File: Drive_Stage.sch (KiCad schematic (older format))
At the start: 34 parts, among them U1 DRV8323SRTAT, U2 24LC01

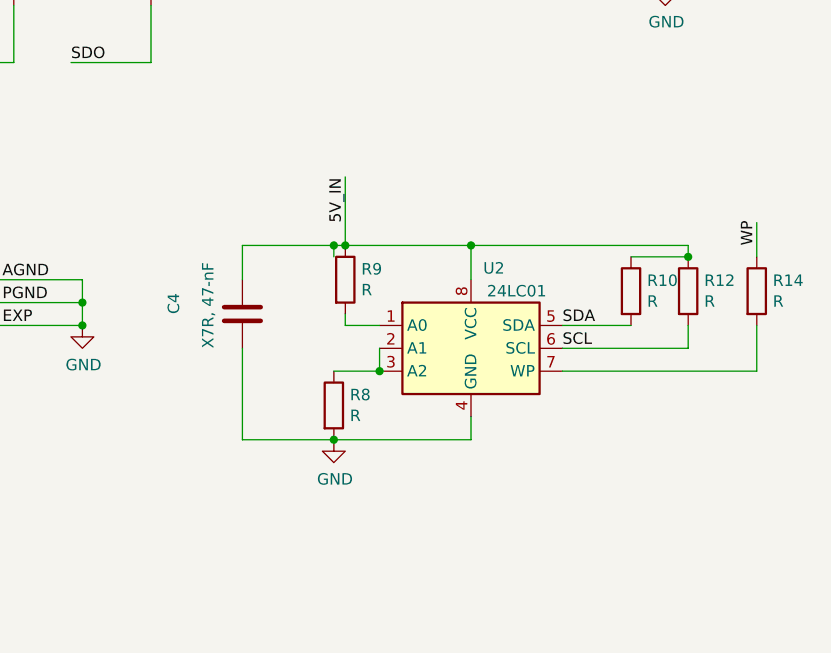
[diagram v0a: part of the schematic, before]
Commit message: update pcb layout
set board cutout
update eeprom footporint
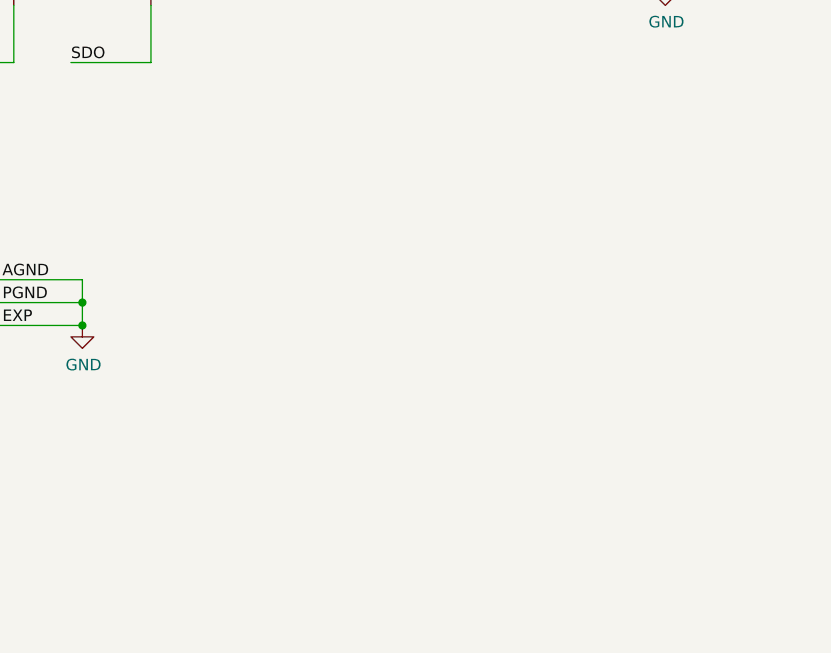
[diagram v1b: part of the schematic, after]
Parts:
- removed C4: X7R, 47-nF, Capacitor_SMD:C_0603_1608Metric_Pad1.05x0.95mm_HandSolder, symbol Device:C
- removed R10, R12, R14, R8, R9: R, Resistor_SMD:R_0603_1608Metric_Pad1.05x0.95mm_HandSolder, symbol Device:R
- removed U2: 24LC01, Package_DFN_QFN:DFN-8-1EP_2x3mm_P0.5mm_EP0.61x2.2mm, symbol Memory_EEPROM:24LC01
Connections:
- wire segments 161 -> 137
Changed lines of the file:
@@
 	1    0    0    -1
 $EndComp
-$Comp
-L Memory_EEPROM:24LC01 U2
-U 1 1 61329F00
-P 9750 4800
-F 0 "U2" H 9850 5150 50  0000 C CNN
-F 1 "24LC01" H 9950 5050 50  0000 C CNN
-F 2 "Package_DFN_QFN:DFN-8-1EP_2x3mm_P0.5mm_EP0.61x2.2mm" H 9750 4800 50  0001 C CNN
-F 3 "http://ww1.microchip.com/downloads/en/DeviceDoc/21711J.pdf" H 9750 4800 50  0001 C CNN
-	1    9750 4800
-	1    0    0    -1
-$EndComp
-$Comp
-L Device:R R9
-U 1 1 61330843
-P 9200 4500
-F 0 "R9" H 9270 4546 50  0000 L CNN
-F 1 "R" H 9270 4455 50  0000 L CNN
-F 2 "Resistor_SMD:R_0603_1608Metric_Pad1.05x0.95mm_HandSolder" V 9130 4500 50  0001 C CNN
-F 3 "~" H 9200 4500 50  0001 C CNN
-	1    9200 4500
-	1    0    0    -1
-$EndComp
-Wire Wire Line
-	9350 4700 9200 4700
-Wire Wire Line
-	9200 4700 9200 4650
-Text Label 9200 4250 1    50   ~ 0
-5V_IN
-Wire Wire Line
-	9350 4800 9350 4900
-Wire Wire Line
-	9350 4900 9150 4900
-Connection ~ 9350 4900
-$Comp
-L Device:R R8
-U 1 1 6134BB6C
-P 9150 5050
-F 0 "R8" H 9220 5096 50  0000 L CNN
-F 1 "R" H 9220 5005 50  0000 L CNN
-F 2 "Resistor_SMD:R_0603_1608Metric_Pad1.05x0.95mm_HandSolder" V 9080 5050 50  0001 C CNN
-F 3 "~" H 9150 5050 50  0001 C CNN
-	1    9150 5050
-	1    0    0    -1
-$EndComp
-$Comp
-L power:GND #PWR06
-U 1 1 6134BF6A
-P 9150 5200
-F 0 "#PWR06" H 9150 4950 50  0001 C CNN
-F 1 "GND" H 9155 5027 50  0000 C CNN
-F 2 "" H 9150 5200 50  0001 C CNN
-F 3 "" H 9150 5200 50  0001 C CNN
-	1    9150 5200
-	1    0    0    -1
-$EndComp
-$Comp
-L Device:R R10
-U 1 1 6134C3A9
-P 10450 4550
-F 0 "R10" H 10520 4596 50  0000 L CNN
-F 1 "R" H 10520 4505 50  0000 L CNN
-F 2 "Resistor_SMD:R_0603_1608Metric_Pad1.05x0.95mm_HandSolder" V 10380 4550 50  0001 C CNN
-F 3 "~" H 10450 4550 50  0001 C CNN
-	1    10450 4550
-	1    0    0    -1
-$EndComp
-$Comp
-L Device:R R12
-U 1 1 6134C69D
-P 10700 4550
-F 0 "R12" H 10770 4596 50  0000 L CNN
-F 1 "R" H 10770 4505 50  0000 L CNN
-F 2 "Resistor_SMD:R_0603_1608Metric_Pad1.05x0.95mm_HandSolder" V 10630 4550 50  0001 C CNN
-F 3 "~" H 10700 4550 50  0001 C CNN
-	1    10700 4550
-	1    0    0    -1
-$EndComp
-Wire Wire Line
-	10150 4700 10450 4700
-Wire Wire Line
-	10150 4800 10700 4800
-Wire Wire Line
-	10700 4800 10700 4700
-Connection ~ 10700 4400
-Wire Wire Line
-	10700 4400 10450 4400
-Wire Wire Line
-	9200 4350 9750 4350
-Wire Wire Line
-	10700 4350 10700 4400
-Connection ~ 9200 4350
 Text Label 9450 2450 1    50   ~ 0
 5V_IN
@@
 Text Label 3050 6500 0    50   ~ 0
 GHB
-$Comp
-L Device:C C4
-U 1 1 614ED686
-P 8750 4650
-F 0 "C4" V 8450 4650 50  0000 L CNN
-F 1 "X7R, 47-nF" V 8600 4500 50  0000 L CNN
-F 2 "Capacitor_SMD:C_0603_1608Metric_Pad1.05x0.95mm_HandSolder" H 8788 4500 50  0001 C CNN
-F 3 "~" H 8750 4650 50  0001 C CNN
-	1    8750 4650
-	1    0    0    -1
-$EndComp
-Wire Wire Line
-	9150 4400 9150 4350
-Wire Wire Line
-	9150 4350 9200 4350
-Wire Wire Line
-	8750 4500 8750 4350
-Wire Wire Line
-	8750 4350 9150 4350
-Connection ~ 9150 4350
-Wire Wire Line
-	8750 4800 8750 5200
-Wire Wire Line
-	8750 5200 9150 5200
-Connection ~ 9150 5200
 Text Label 5900 2250 2    50   ~ 0
 5V_IN_RAW
@@
 	1    0    0    -1
 $EndComp
-Wire Wire Line
-	9750 4500 9750 4350
-Connection ~ 9750 4350
-Wire Wire Line
-	9750 4350 10700 4350
-Wire Wire Line
-	9750 5200 9750 5100
-Wire Wire Line
-	9150 5200 9750 5200
 Text Label 5850 4450 0    50   ~ 0
 VM_Protected
@@
 	6300 2250 6750 2250
 Connection ~ 6750 2250
-Text Label 10150 4700 0    50   ~ 0
-SDA
-Text Label 10150 4800 0    50   ~ 0
-SCL
 Text Label 1400 4750 0    50   ~ 0
 SDA
@@
 	1350 4750 1700 4750
 Wire Wire Line
-	9200 4050 9200 4350
-Wire Wire Line
 	1700 4850 1350 4850
 Text Label 1400 4950 0    50   ~ 0
@@
 Wire Wire Line
 	1700 4950 1350 4950
-$Comp
-L Device:R R14
-U 1 1 61C58061
-P 11000 4550
-F 0 "R14" H 11070 4596 50  0000 L CNN
-F 1 "R" H 11070 4505 50  0000 L CNN
-F 2 "Resistor_SMD:R_0603_1608Metric_Pad1.05x0.95mm_HandSolder" V 10930 4550 50  0001 C CNN
-F 3 "~" H 11000 4550 50  0001 C CNN
-	1    11000 4550
-	1    0    0    -1
-$EndComp
-Wire Wire Line
-	11000 4900 11000 4700
-Text Label 11000 4350 1    50   ~ 0
-WP
-Wire Wire Line
-	11000 4400 11000 4250
-Wire Wire Line
-	10150 4900 11000 4900
 Wire Wire Line
 	3300 4900 3300 5050

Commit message: add production files
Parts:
- added D5: D_Schottky, Diode_SMD:D_0603_1608Metric_Pad1.05x0.95mm_HandSolder, symbol Device:D_Schottky
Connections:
- net labels added: 5V, EEPROM_SCL, EEPROM_SDA, EEPROM_WP
- net labels removed: SCL, SDA, WP
- wire segments 137 -> 139
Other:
- moved on the sheet: F2
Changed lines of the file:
@@
 	6750 2250 6750 2750
 Wire Wire Line
-	6750 2250 7750 2250
+	6750 2250 7100 2250
 Connection ~ 7750 2250
 Wire Wire Line
@@
 Text Label 3050 6500 0    50   ~ 0
 GHB
-Text Label 5900 2250 2    50   ~ 0
+Text Label 5500 2250 2    50   ~ 0
 5V_IN_RAW
 $Comp
 L Device:Fuse F2
 U 1 1 615065CC
-P 6100 2250
-F 0 "F2" V 5950 2250 50  0000 C CNN
-F 1 "Fuse" V 5994 2250 50  0000 C CNN
-F 2 "Fuse:Fuse_0603_1608Metric_Pad1.05x0.95mm_HandSolder" V 6030 2250 50  0001 C CNN
-F 3 "~" H 6100 2250 50  0001 C CNN
-	1    6100 2250
+P 5700 2250
+F 0 "F2" V 5550 2250 50  0000 C CNN
+F 1 "Fuse" V 5594 2250 50  0000 C CNN
+F 2 "Fuse:Fuse_0603_1608Metric_Pad1.05x0.95mm_HandSolder" V 5630 2250 50  0001 C CNN
+F 3 "~" H 5700 2250 50  0001 C CNN
+	1    5700 2250
 	0    1    1    0
 $EndComp
 Wire Wire Line
-	5550 2250 5950 2250
-Wire Wire Line
-	6250 2250 6300 2250
+	5150 2250 5550 2250
 $Comp
 L Device:R R7
@@
 	6300 2250 6750 2250
 Connection ~ 6750 2250
-Text Label 1400 4750 0    50   ~ 0
-SDA
-Text Label 1400 4850 0    50   ~ 0
-SCL
 Wire Wire Line
 	1350 4750 1700 4750
 Wire Wire Line
 	1700 4850 1350 4850
-Text Label 1400 4950 0    50   ~ 0
-WP
 Wire Wire Line
 	1700 4950 1350 4950
@@
 Wire Wire Line
 	7950 1250 8850 1250
+Text HLabel 1360 4750 0    50   Input ~ 0
+EEPROM_SDA
+Text HLabel 1350 4850 0    50   Input ~ 0
+EEPROM_SCL
+Text HLabel 1350 4950 0    50   Input ~ 0
+EEPROM_WP
+Text HLabel 7100 2100 1    50   Input ~ 0
+5V
+$Comp
+L Device:D_Schottky D5
+U 1 1 610C911D
+P 6000 2250
+F 0 "D5" H 6000 2034 50  0000 C CNN
+F 1 "D_Schottky" H 6000 2125 50  0000 C CNN
+F 2 "Diode_SMD:D_0603_1608Metric_Pad1.05x0.95mm_HandSolder" H 6000 2250 50  0001 C CNN
+F 3 "~" H 6000 2250 50  0001 C CNN
+	1    6000 2250
+	-1   0    0    1
+$EndComp
+Wire Wire Line
+	6150 2250 6300 2250
+Wire Wire Line
+	7100 2250 7100 2100
+Connection ~ 7100 2250
+Wire Wire Line
+	7100 2250 7750 2250
 $EndSCHEMATC

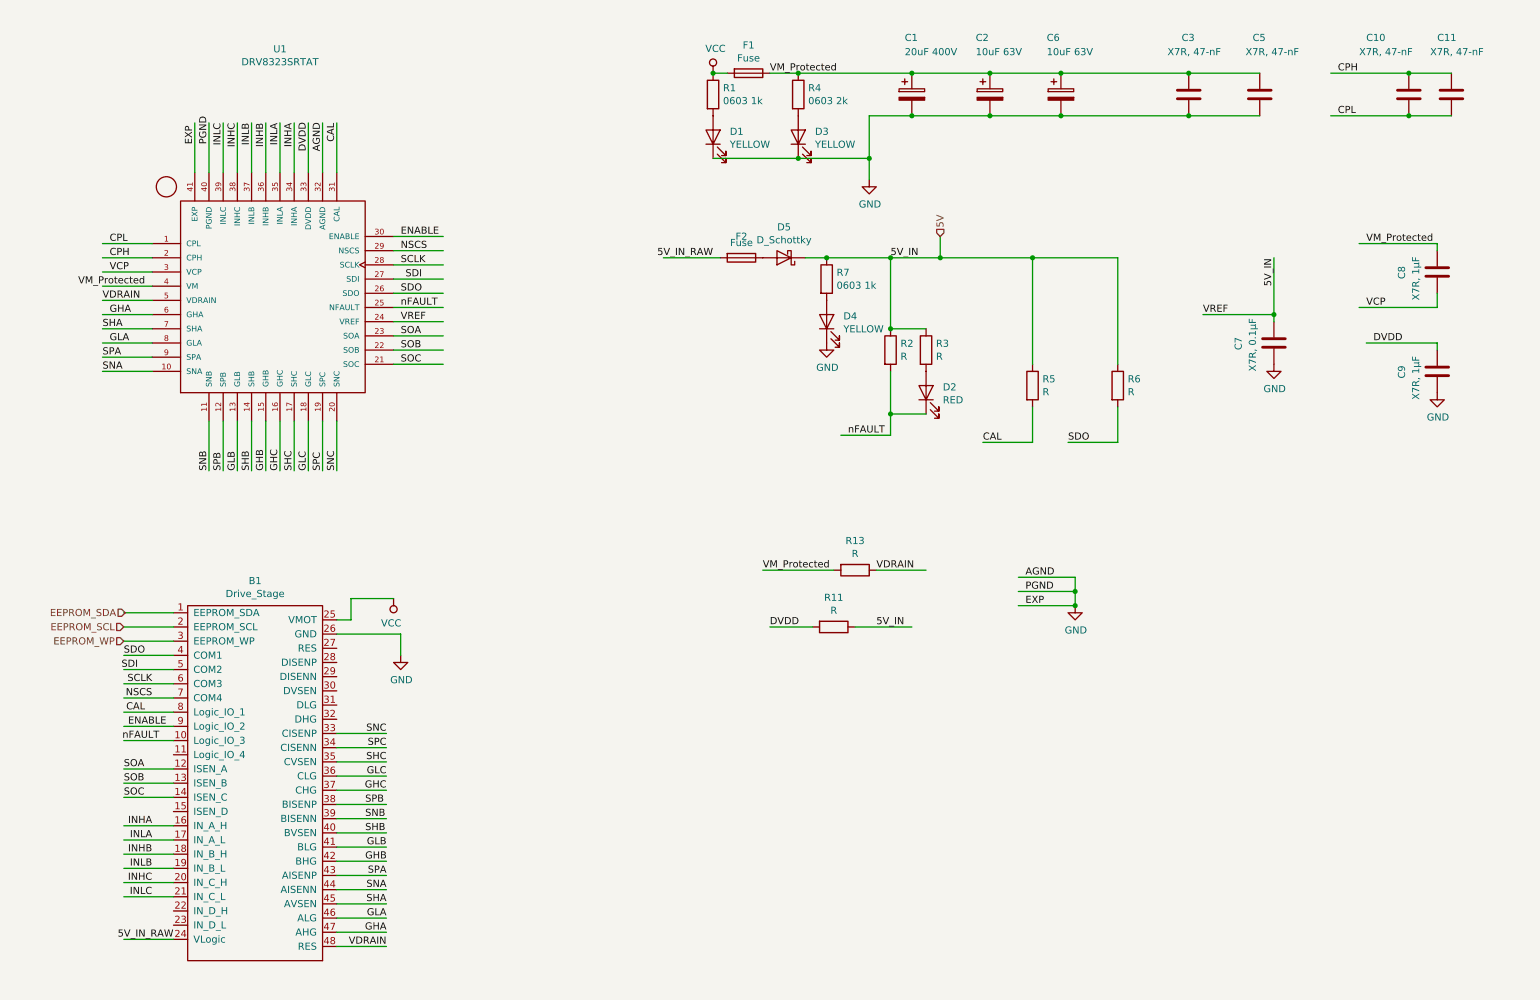
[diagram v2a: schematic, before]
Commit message: add voltage supply sense resistors
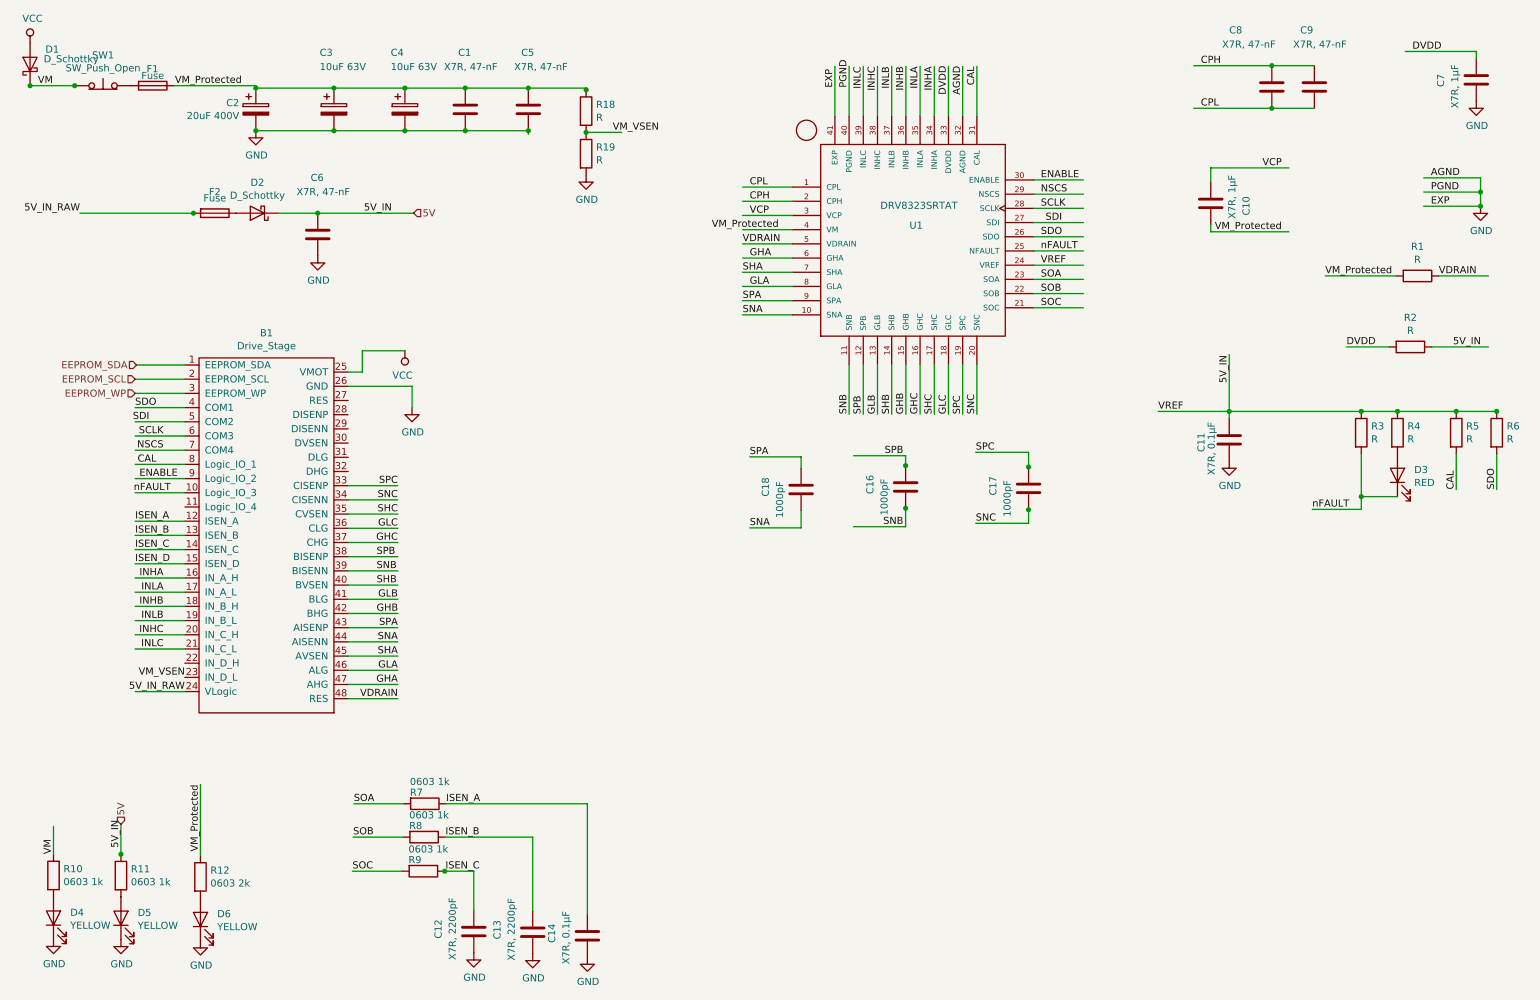
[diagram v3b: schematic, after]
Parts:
- added C12, C13: X7R, 2200pF, Capacitor_SMD:C_0603_1608Metric_Pad1.05x0.95mm_HandSolder, symbol Device:C
- added C14: X7R, 0.1µF, Capacitor_SMD:C_0603_1608Metric_Pad1.05x0.95mm_HandSolder, symbol Device:C
- added C16, C17, C18: 1000pF, Capacitor_SMD:C_0603_1608Metric_Pad1.05x0.95mm_HandSolder, symbol Device:C
- added C6: X7R, 47-nF, Capacitor_SMD:C_0603_1608Metric_Pad1.05x0.95mm_HandSolder, symbol Device:C
- added D1: D_Schottky, Diode_SMD:D_0603_1608Metric_Pad1.05x0.95mm_HandSolder, symbol Device:D_Schottky
- added R18, R19: R, Resistor_SMD:R_0603_1608Metric_Pad1.05x0.95mm_HandSolder, symbol Device:R
- added R7, R8, R9: 0603 1k, Resistor_SMD:R_0603_1608Metric_Pad1.05x0.95mm_HandSolder, symbol Device:R
- added SW1: SW_Push_Open, Button_Switch_SMD:SW_DIP_SPSTx01_Slide_6.7x4.1mm_W6.73mm_P2.54mm_LowProfile_JPin, symbol Switch:SW_Push_Open
- renumbered C3 to C1, C8 to C10, C7 to C11, C1 to C2, C2 to C3, C6 to C4, C9 to C7, C10 to C8, C11 to C9, D5 to D2, D2 to D3, D1 to D4, D4 to D5, D3 to D6, R13 to R1, R1 to R10, R7 to R11, R4 to R12, R11 to R2, R2 to R3, R3 to R4
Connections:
- net labels added: ISEN_A, ISEN_B, ISEN_C, ISEN_D, VM, VM_VSEN
- wire segments 139 -> 172
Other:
- moved on the sheet: B1, C1, C10, C11, C2, C3, C4, C5, C7, C8, C9, D2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

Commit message: move VMsen to pin 8
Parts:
- B1: symbol sDrive_Carriers:Drive_Stage -> sDrive1-rescue:Drive_Stage-sDrive_Carriers
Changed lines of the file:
@@
 	2930 4555 3280 4555
 $Comp
-L sDrive_Carriers:Drive_Stage B1
+L sDrive1-rescue:Drive_Stage-sDrive_Carriers B1
 U 1 1 612B38E9
 P 2330 3905
+AR Path="/612B38E9" Ref="B1"  Part="1"
+AR Path="/60E74488/612B38E9" Ref="B1"  Part="1"
 F 0 "B1" H 2355 5030 50  0000 C CNN
 F 1 "Drive_Stage" H 2355 4939 50  0000 C CNN
@@
 Text Label 4793 1367 0    50   ~ 0
 VM_VSEN
-Text Label 1780 5205 2    50   ~ 0
+Text Label 1780 4005 2    50   ~ 0
 VM_VSEN
 Connection ~ 4606 1367
